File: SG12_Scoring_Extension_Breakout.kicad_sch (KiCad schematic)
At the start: 19 parts, among them J1 RJ45, J2 Barrel_Jack_MountingPin, J3 Barrel_Jack_MountingPin, J4 Barrel_Jack_MountingPin, J5 Barrel_Jack_MountingPin, J6 Barrel_Jack_MountingPin, J8 Conn_02x08_Odd_Even, Q1 IRF4905, Q2 IRF4905, Q3 IRF4905, Q4 IRF4905

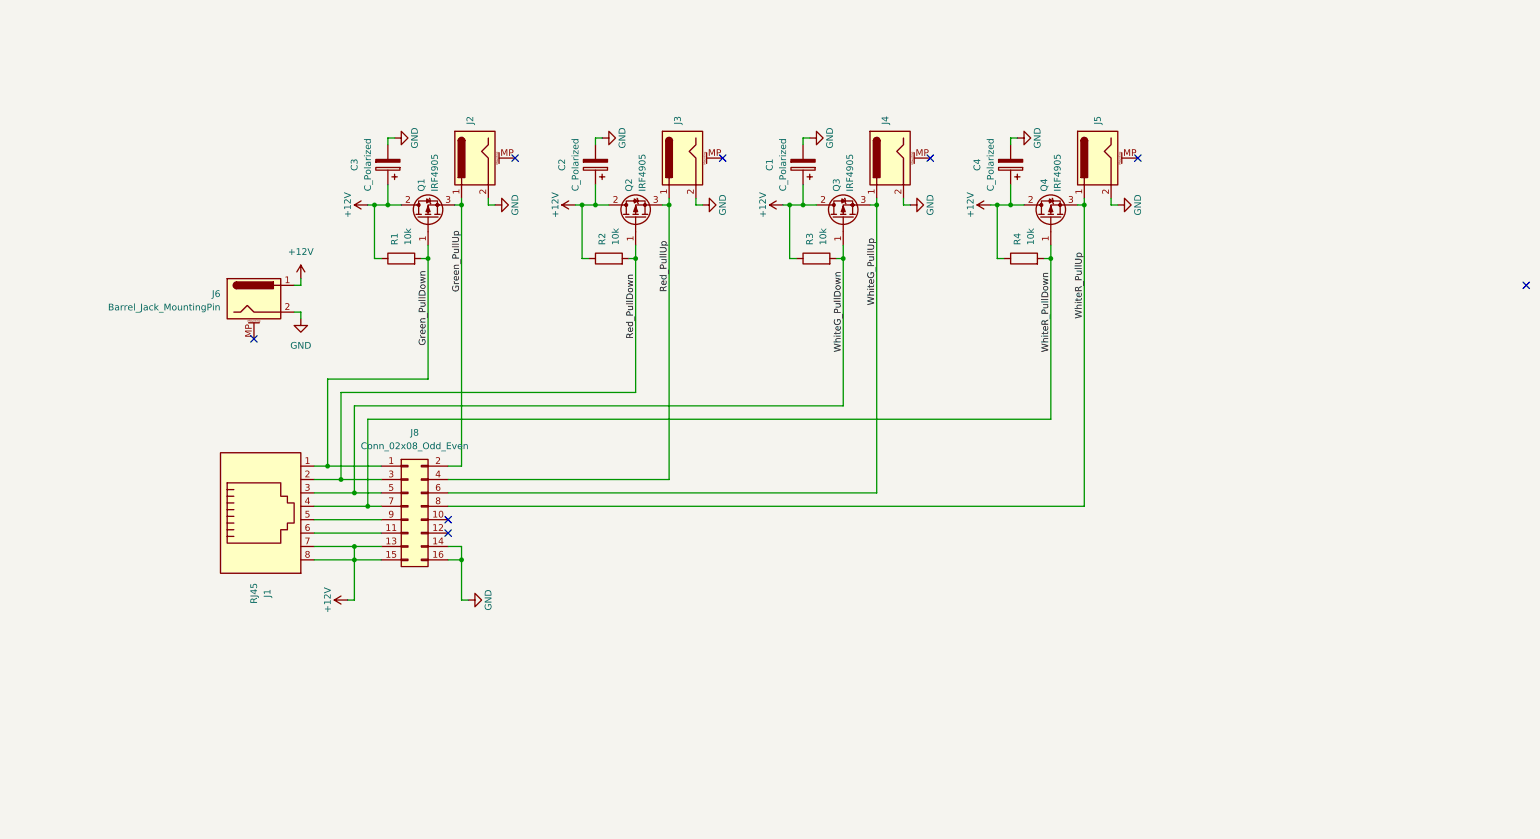
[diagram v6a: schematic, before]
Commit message: Updated schematic with extra connections
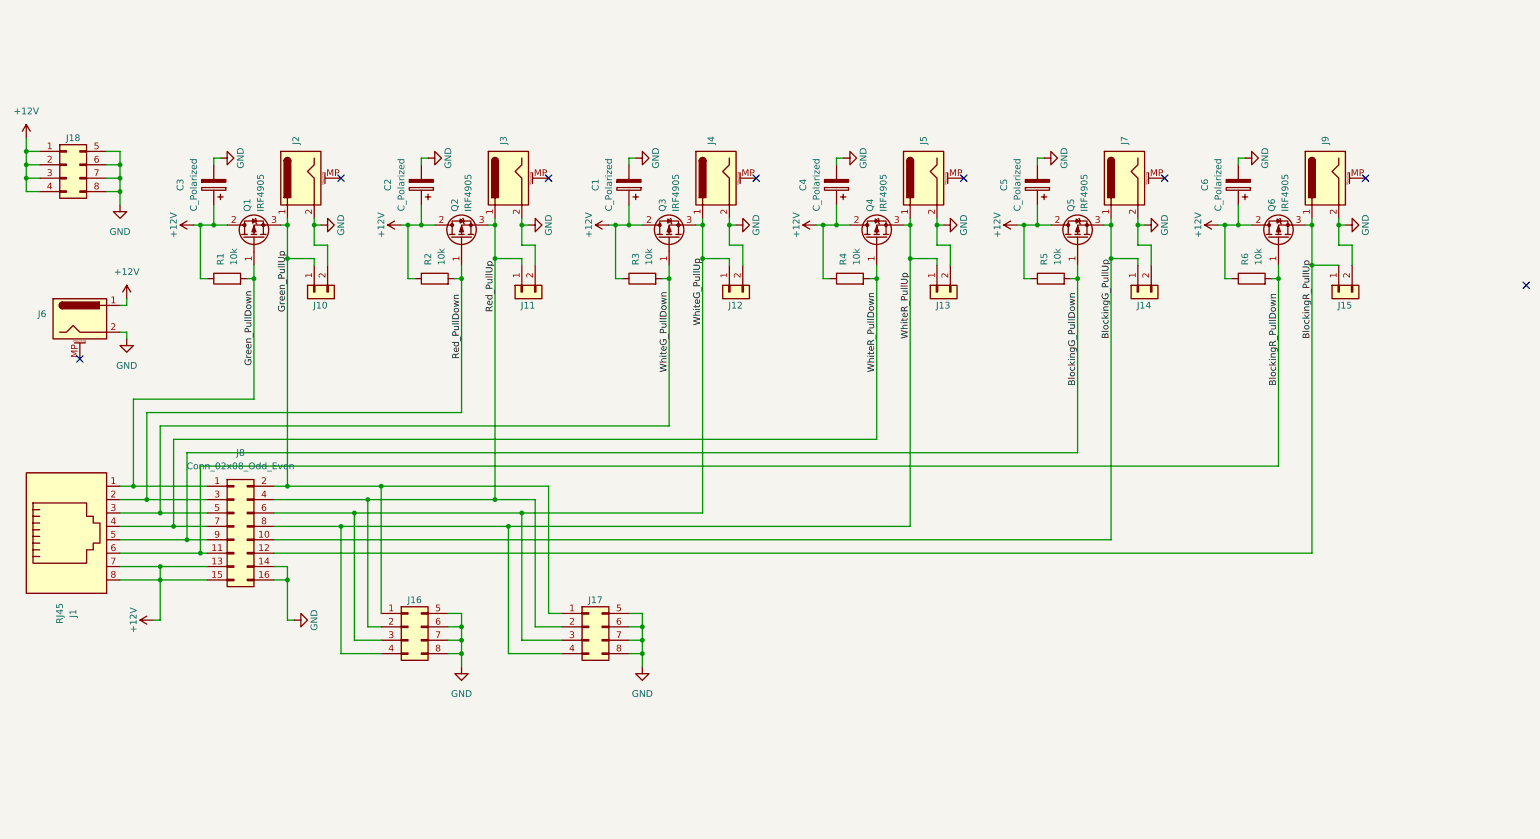
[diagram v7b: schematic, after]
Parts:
- added C5, C6: C_Polarized, Capacitor_THT:CP_Radial_D6.3mm_P2.50mm, symbol Device:C_Polarized
- added J10, J11, J12, J13, J14, J15: Conn_01x02, Connector_Phoenix_MSTB:PhoenixContact_MSTBA_2,5_2-G-5,08_1x02_P5.08mm_Horizontal, symbol Connector_Generic:Conn_01x02
- added J16, J17: Conn_02x04_Top_Bottom, Connector_Molex:Molex_Mini-Fit_Jr_5569-08A2_2x04_P4.20mm_Horizontal, symbol Connector_Generic:Conn_02x04_Top_Bottom
- added J18: Conn_02x04_Top_Bottom, Connector_Phoenix_MSTB:PhoenixContact_MSTBA_2,5_2-G-5,08_1x02_P5.08mm_Horizontal, symbol Connector_Generic:Conn_02x04_Top_Bottom
- added J7, J9: Barrel_Jack_MountingPin, Library:BarrelJack_GCT_DCJ200-10-A_Horizontal, symbol Connector:Barrel_Jack_MountingPin
- added Q5, Q6: IRF4905, Package_TO_SOT_THT:TO-220-3_Vertical, symbol Transistor_FET:IRF4905
- added R5, R6: 10k, Resistor_THT:R_Axial_DIN0207_L6.3mm_D2.5mm_P10.16mm_Horizontal, symbol Device:R
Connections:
- net +12V: now also C5.1, C6.1, J18.1 (Pin_1), J18.2 (Pin_2), J18.3 (Pin_3), J18.4 (Pin_4), Q5.2 (D), Q6.2 (D), R5.1, R6.1
- net GND: now also C5.2, C6.2, J10.2 (Pin_2), J11.2 (Pin_2), J12.2 (Pin_2), J13.2 (Pin_2), J14.2 (Pin_2), J15.2 (Pin_2), J16.5 (Pin_5), J16.6 (Pin_6), J16.7 (Pin_7), J16.8 (Pin_8), J17.5 (Pin_5), J17.6 (Pin_6), J17.7 (Pin_7), J17.8 (Pin_8), J18.5 (Pin_5), J18.6 (Pin_6), J18.7 (Pin_7), J18.8 (Pin_8), J7.2, J9.2
- net Green_PullUp: now also J10.1 (Pin_1), J16.1 (Pin_1), J17.1 (Pin_1)
- net Red_PullUp: now also J11.1 (Pin_1), J16.2 (Pin_2), J17.2 (Pin_2)
- net WhiteG_PullUp: now also J12.1 (Pin_1), J16.3 (Pin_3), J17.3 (Pin_3)
- net WhiteR_PullUp: now also J13.1 (Pin_1), J16.4 (Pin_4), J17.4 (Pin_4)
- net BlockingG_PullUp: now reaches J8.10 (Pin_10)
- net BlockingG_PullUp: now also J14.1 (Pin_1), J7.1, Q5.3 (S)
- net BlockingR_PullDown: now reaches J1.6, J8.11 (Pin_11)
- net BlockingR_PullDown: now also Q6.1 (G), R6.2
- net BlockingR_PullUp: now reaches J8.12 (Pin_12)
- net BlockingR_PullUp: now also J15.1 (Pin_1), J9.1, Q6.3 (S)
- net BlockingG_PullDown: now reaches J1.5, J8.9 (Pin_9)
- net BlockingG_PullDown: now also Q5.1 (G), R5.2
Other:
- moved on the sheet: C1, C2, C3, C4, J1, J2, J3, J4, J5, J6, J8, Q1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

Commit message: Forgot connector
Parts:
- added J19: Conn_01x02, Connector_Phoenix_MSTB:PhoenixContact_MSTBA_2,5_2-G-5,08_1x02_P5.08mm_Horizontal, symbol Connector_Generic:Conn_01x02
- J18: footprint Connector_Phoenix_MSTB:PhoenixContact_MSTBA_2,5_2-G-5,08_1x02_P5.08mm_Horizontal -> Connector_Molex:Molex_Mini-Fit_Jr_5569-08A2_2x04_P4.20mm_Horizontal
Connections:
- net +12V: now also J19.1 (Pin_1)
- net GND: now also J19.2 (Pin_2)
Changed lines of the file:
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@@
 (kicad_sch (version 20230121) (generator eeschema)
   (paper "A4")
+  (junction (at 20.32 60.96) (diameter 0) (color 0 0 0 0)
+  )
   (junction (at 69.85 116.84) (diameter 0) (color 0 0 0 0)
   )
@@
   )
   (junction (at 109.22 119.38) (diameter 0) (color 0 0 0 0)
+  )
+  (junction (at 38.1 64.77) (diameter 0) (color 0 0 0 0)
   )
   (junction (at 85.09 119.38) (diameter 0) (color 0 0 0 0)
@@
     (stroke (width 0) (type default))
   )
+  (wire (pts (xy 30.48 64.77) (xy 38.1 64.77))
+    (stroke (width 0) (type default))
+  )
   (wire (pts (xy 219.71 110.49) (xy 219.71 77.47))
     (stroke (width 0) (type default))
@@
     (stroke (width 0) (type default))
   )
+  (wire (pts (xy 27.94 64.77) (xy 20.32 64.77))
+    (stroke (width 0) (type default))
+  )
   (wire (pts (xy 38.1 55.88) (xy 38.1 58.42))
     (stroke (width 0) (type default))
@@
     (stroke (width 0) (type default))
   )
+  (wire (pts (xy 27.94 68.58) (xy 27.94 64.77))
+    (stroke (width 0) (type default))
+  )
   (wire (pts (xy 50.8 110.49) (xy 219.71 110.49))
     (stroke (width 0) (type default))
@@
     (stroke (width 0) (type default))
   )
+  (wire (pts (xy 20.32 64.77) (xy 20.32 60.96))
+    (stroke (width 0) (type default))
+  )
   (wire (pts (xy 247.65 77.47) (xy 248.92 77.47))
     (stroke (width 0) (type default))
@@
     (stroke (width 0) (type default))
   )
-  (wire (pts (xy 38.1 60.96) (xy 38.1 63.5))
+  (wire (pts (xy 38.1 60.96) (xy 38.1 64.77))
     (stroke (width 0) (type default))
   )
@@
     (stroke (width 0) (type default))
   )
+  (wire (pts (xy 38.1 64.77) (xy 38.1 66.04))
+    (stroke (width 0) (type default))
+  )
   (wire (pts (xy 62.23 77.47) (xy 63.5 77.47))
     (stroke (width 0) (type default))
@@
   )
   (wire (pts (xy 121.92 148.59) (xy 111.76 148.59))
+    (stroke (width 0) (type default))
+  )
+  (wire (pts (xy 30.48 68.58) (xy 30.48 64.77))
     (stroke (width 0) (type default))
   )
@@
       (effects (font (size 1.27 1.27)) hide)
     )
-    (property "Footprint" "Connector_Phoenix_MSTB:PhoenixContact_MSTBA_2,5_2-G-5,08_1x02_P5.08mm_Horizontal" (at 27.94 55.88 0)
+    (property "Footprint" "Connector_Molex:Molex_Mini-Fit_Jr_5569-08A2_2x04_P4.20mm_Horizontal" (at 27.94 55.88 0)
       (effects (font (size 1.27 1.27)) hide)
     )
@@
     )
   )
+  (symbol (lib_id "Connector_Generic:Conn_01x02") (at 27.94 73.66 90) (mirror x) (unit 1)
+    (in_bom yes) (on_board yes) (dnp no)
+    (property "Reference" "J19" (at 30.48 76.2 90)
+      (effects (font (size 1.27 1.27)) (justify left))
+    )
+    (property "Value" "Conn_01x02" (at 25.4 74.93 90)
+      (effects (font (size 1.27 1.27)) (justify left) hide)
+    )
+    (property "Footprint" "Connector_Phoenix_MSTB:PhoenixContact_MSTBA_2,5_2-G-5,08_1x02_P5.08mm_Horizontal" (at 27.94 73.66 0)
+      (effects (font (size 1.27 1.27)) hide)
+    )
+    (property "Datasheet" "~" (at 27.94 73.66 0)
+      (effects (font (size 1.27 1.27)) hide)
+    )
+    (pin "1")
+    (pin "2")
+    (instances
+      (project "SG12_Scoring_Extension_Breakout"
+        (path "/d3a18a1f-0030-40cf-934c-0abb5a098964"
+          (reference "J19") (unit 1)
+        )
+      )
+    )
+  )
   (symbol (lib_id "power:GND") (at 102.87 151.13 0) (unit 1)
     (in_bom yes) (on_board yes) (dnp no) (fields_autoplaced)
@@
     )
   )
-  (symbol (lib_id "power:GND") (at 38.1 63.5 0) (unit 1)
+  (symbol (lib_id "power:GND") (at 38.1 66.04 0) (unit 1)
     (in_bom yes) (on_board yes) (dnp no) (fields_autoplaced)
-    (property "Reference" "#PWR025" (at 38.1 69.85 0)
-      (effects (font (size 1.27 1.27)) hide)
-    )
-    (property "Value" "GND" (at 38.1 68.58 0)
-      (effects (font (size 1.27 1.27)))
-    )
-    (property "Footprint" "" (at 38.1 63.5 0)
-      (effects (font (size 1.27 1.27)) hide)
-    )
-    (property "Datasheet" "" (at 38.1 63.5 0)
-      (effects (font (size 1.27 1.27)) hide)
-    )
+    (property "Reference" "#PWR025" (at 38.1 72.39 0)
+      (effects (font (size 1.27 1.27)) hide)
+    )
+    (property "Value" "GND" (at 38.1 71.12 0)
+      (effects (font (size 1.27 1.27)))
+    )
+    (property "Footprint" "" (at 38.1 66.04 0)
+      (effects (font (size 1.27 1.27)) hide)
+    )
+    (property "Datasheet" "" (at 38.1 66.04 0)
+      (effects (font (size 1.27 1.27)) hide)
+    )
